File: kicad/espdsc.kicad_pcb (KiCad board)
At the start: 2 copper layers, 58.4 x 35.3 mm, 15 parts, among them J1 RJ45, P1 USB_B, SW1 Reset, SW2 Prog, U1 ESP-12E, U2 MCP1825S-3302E/DB, U3 TXB0104

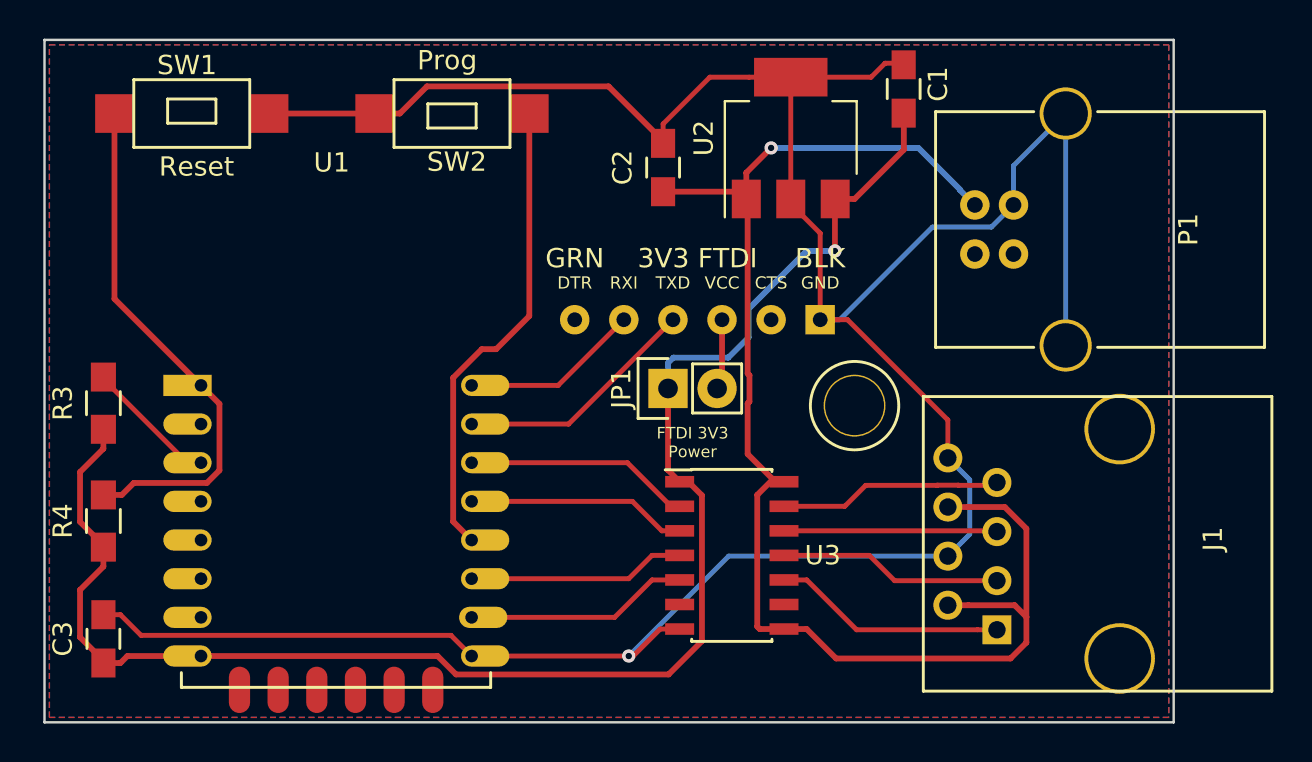
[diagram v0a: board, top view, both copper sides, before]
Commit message: update design for v1.0 release
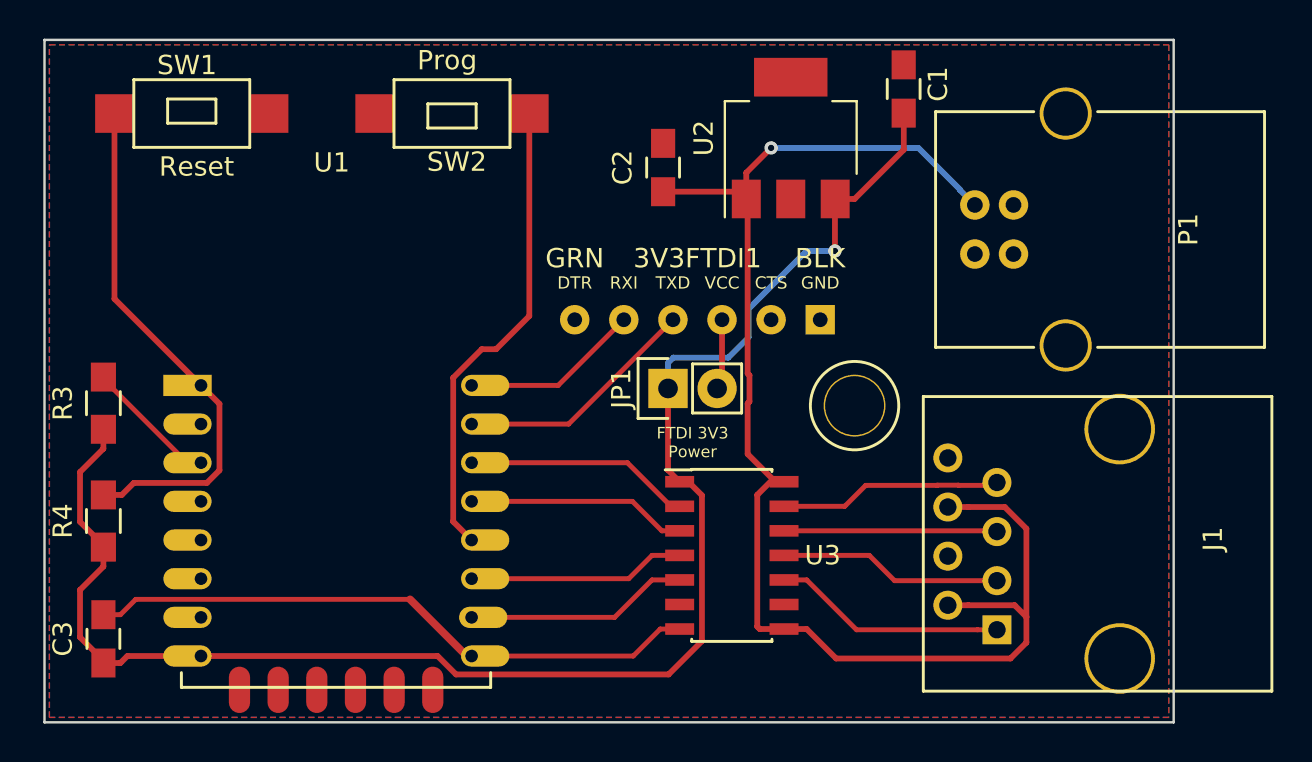
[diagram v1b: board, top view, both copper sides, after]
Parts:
- 3V3FTDI1: renamed from 3V3 FTDI
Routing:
- net GND: track 147.3 -> 31.9 mm, vias 1 -> 0
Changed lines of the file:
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@@
     (thickness 1.6)
     (drawings 6)
-    (tracks 166)
+    (tracks 131)
     (zones 0)
     (modules 15)
@@
   )
   (setup
-    (last_trace_width 0.3)
+    (last_trace_width 0.254)
     (user_trace_width 0.1524)
     (user_trace_width 0.2)
@@
   (net 15 "Net-(R3-Pad2)")
   (net 16 "Net-(R4-Pad2)")
-  (net 17 "Net-(CONN1-Pad4)")
+  (net 17 "Net-(3V3FTDI1-Pad4)")
   (net_class Default "Dit is de standaard class."
     (clearance 0.254)
@@
     (add_net +5V)
     (add_net GND)
-    (add_net "Net-(CONN1-Pad4)")
+    (add_net "Net-(3V3FTDI1-Pad4)")
     (add_net "Net-(J1-Pad1)")
     (add_net "Net-(J1-Pad3)")
@@
   (module synfinatic:FTDIHeader (layer F.Cu)
     (at 196.342 101.854)
-    (fp_text reference "3V3 FTDI" (at 0 -3.175) (layer F.SilkS)
+    (fp_text reference 3V3FTDI1 (at 0 -3.175) (layer F.SilkS)
       (effects (font (size 1 1) (thickness 0.15)))
     )
@@
       (net 5 RXD))
     (pad 4 thru_hole circle (at 1.27 0) (size 1.524 1.524) (drill 0.762) (layers *.Cu *.Mask)
-      (net 17 "Net-(CONN1-Pad4)"))
+      (net 17 "Net-(3V3FTDI1-Pad4)"))
     (pad 5 thru_hole circle (at 3.81 0) (size 1.524 1.524) (drill 0.762) (layers *.Cu *.Mask))
     (pad 6 thru_hole rect (at 6.35 0) (size 1.524 1.524) (drill 0.762) (layers *.Cu *.Mask)
@@
       (net 1 +3V3))
     (pad 2 thru_hole oval (at 0 2.54 90) (size 2.032 2.032) (drill 1.016) (layers *.Cu *.Mask)
-      (net 17 "Net-(CONN1-Pad4)"))
+      (net 17 "Net-(3V3FTDI1-Pad4)"))
     (model Pin_Headers.3dshapes/Pin_Header_Straight_1x02.wrl
       (at (xyz 0 -0.05 0))
@@
   (segment (start 166.849 119.252) (end 170.658 119.252) (width 0.3) (layer F.Cu) (net 1))
   (segment (start 166.487 119.614) (end 166.849 119.252) (width 0.3) (layer F.Cu) (net 1))
-  (segment (start 202.692 101.854) (end 204.107309 101.854) (width 0.254) (layer F.Cu) (net 2))
-  (segment (start 204.107309 101.854) (end 209.296 107.042691) (width 0.254) (layer F.Cu) (net 2))
-  (segment (start 209.296 107.042691) (end 209.296 109.0041) (width 0.254) (layer F.Cu) (net 2))
-  (segment (start 194.564 92.73) (end 194.564 92.605) (width 0.3) (layer F.Cu) (net 2))
-  (segment (start 194.564 92.605) (end 191.740999 89.781999) (width 0.3) (layer F.Cu) (net 2))
-  (segment (start 191.740999 89.781999) (end 182.346001 89.781999) (width 0.3) (layer F.Cu) (net 2))
-  (segment (start 182.346001 89.781999) (end 180.942 91.186) (width 0.3) (layer F.Cu) (net 2))
-  (segment (start 180.942 91.186) (end 179.642 91.186) (width 0.3) (layer F.Cu) (net 2))
-  (segment (start 174.18 91.186) (end 179.642 91.186) (width 0.3) (layer F.Cu) (net 2))
-  (segment (start 201.168 89.306) (end 205.325801 89.306) (width 0.254) (layer F.Cu) (net 2))
-  (segment (start 205.325801 89.306) (end 206.048188 88.583613) (width 0.254) (layer F.Cu) (net 2))
-  (segment (start 206.048188 88.583613) (end 206.584387 88.583613) (width 0.254) (layer F.Cu) (net 2))
-  (segment (start 206.584387 88.583613) (end 207.01 88.158) (width 0.254) (layer F.Cu) (net 2))
-  (segment (start 165.608 117.114) (end 166.487 117.114) (width 0.254) (layer F.Cu) (net 2))
-  (segment (start 166.487 117.114) (end 167.55601 118.18301) (width 0.254) (layer F.Cu) (net 2))
-  (segment (start 167.55601 118.18301) (end 183.58901 118.18301) (width 0.254) (layer F.Cu) (net 2))
-  (segment (start 183.58901 118.18301) (end 184.658 119.252) (width 0.254) (layer F.Cu) (net 2))
-  (segment (start 215.392 91.186) (end 212.69198 93.88602) (width 0.254) (layer B.Cu) (net 2))
-  (segment (start 212.69198 93.88602) (end 212.69198 95.91548) (width 0.254) (layer B.Cu) (net 2))
-  (segment (start 184.658 119.252) (end 192.786 119.252) (width 0.254) (layer F.Cu) (net 2))
-  (segment (start 192.786 119.252) (end 193.02 119.252) (width 0.254) (layer F.Cu) (net 2))
-  (segment (start 209.296 114.0841) (end 197.9539 114.0841) (width 0.254) (layer B.Cu) (net 2))
-  (segment (start 197.9539 114.0841) (end 192.786 119.252) (width 0.254) (layer B.Cu) (net 2))
-  (via (at 192.786 119.252) (size 0.6858) (drill 0.3302) (layers F.Cu B.Cu) (net 2))
-  (segment (start 193.02 119.252) (end 194.416 117.856) (width 0.254) (layer F.Cu) (net 2))
-  (segment (start 194.416 117.856) (end 195.42 117.856) (width 0.254) (layer F.Cu) (net 2))
-  (segment (start 194.564 92.73) (end 194.564 91.726) (width 0.254) (layer F.Cu) (net 2))
-  (segment (start 194.564 91.726) (end 196.984 89.306) (width 0.254) (layer F.Cu) (net 2))
-  (segment (start 196.984 89.306) (end 199.014 89.306) (width 0.254) (layer F.Cu) (net 2))
-  (segment (start 199.014 89.306) (end 201.168 89.306) (width 0.254) (layer F.Cu) (net 2))
-  (segment (start 201.168 89.306) (end 201.168 95.606) (width 0.254) (layer F.Cu) (net 2))
-  (segment (start 202.692 101.854) (end 202.692 97.38) (width 0.254) (layer F.Cu) (net 2))
-  (segment (start 202.692 97.38) (end 201.168 95.856) (width 0.254) (layer F.Cu) (net 2))
-  (segment (start 201.168 95.856) (end 201.168 95.606) (width 0.254) (layer F.Cu) (net 2))
-  (segment (start 212.69198 95.91548) (end 211.548979 97.058481) (width 0.254) (layer B.Cu) (net 2))
-  (segment (start 203.708 101.854) (end 202.692 101.854) (width 0.254) (layer B.Cu) (net 2))
-  (segment (start 208.503519 97.058481) (end 203.708 101.854) (width 0.254) (layer B.Cu) (net 2))
-  (segment (start 211.548979 97.058481) (end 208.503519 97.058481) (width 0.254) (layer B.Cu) (net 2))
-  (segment (start 209.296 109.0041) (end 210.427571 110.135671) (width 0.254) (layer B.Cu) (net 2))
-  (segment (start 210.427571 110.135671) (end 210.427571 112.952529) (width 0.254) (layer B.Cu) (net 2))
-  (segment (start 210.427571 112.952529) (end 210.046569 113.333531) (width 0.254) (layer B.Cu) (net 2))
-  (segment (start 210.046569 113.333531) (end 209.296 114.0841) (width 0.254) (layer B.Cu) (net 2))
-  (segment (start 215.392 91.186) (end 215.392 103.18496) (width 0.254) (layer B.Cu) (net 2))
+  (segment (start 195.42 117.856) (end 194.416 117.856) (width 0.254) (layer F.Cu) (net 2))
+  (segment (start 194.416 117.856) (end 193.02 119.252) (width 0.254) (layer F.Cu) (net 2))
+  (segment (start 193.02 119.252) (end 184.658 119.252) (width 0.254) (layer F.Cu) (net 2))
+  (segment (start 184.403 119.252) (end 181.47199 116.32099) (width 0.4) (layer F.Cu) (net 2))
+  (segment (start 181.47199 116.32099) (end 167.28001 116.32099) (width 0.254) (layer F.Cu) (net 2))
+  (segment (start 167.28001 116.32099) (end 166.487 117.114) (width 0.254) (layer F.Cu) (net 2))
+  (segment (start 166.487 117.114) (end 165.608 117.114) (width 0.254) (layer F.Cu) (net 2))
+  (segment (start 184.658 119.252) (end 184.403 119.252) (width 0.254) (layer F.Cu) (net 2))
   (segment (start 198.868 95.606) (end 198.937648 95.675648) (width 0.3) (layer F.Cu) (net 3))
   (segment (start 198.937648 95.675648) (end 198.937648 104.634046) (width 0.3) (layer F.Cu) (net 3))

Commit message: v1.1 board & code
- Move GPIO2/15 to GPIO14/12 to avoid boot conflict
- Remove level shifter and replace with 4x 150Ohm resistors
- Tweak RJ45 footprint for better fit
- Add pullup for D+ on USB
- Remove 3.3V FTDI jumper
- Move Reset button label
- FTDI no longer can provide power
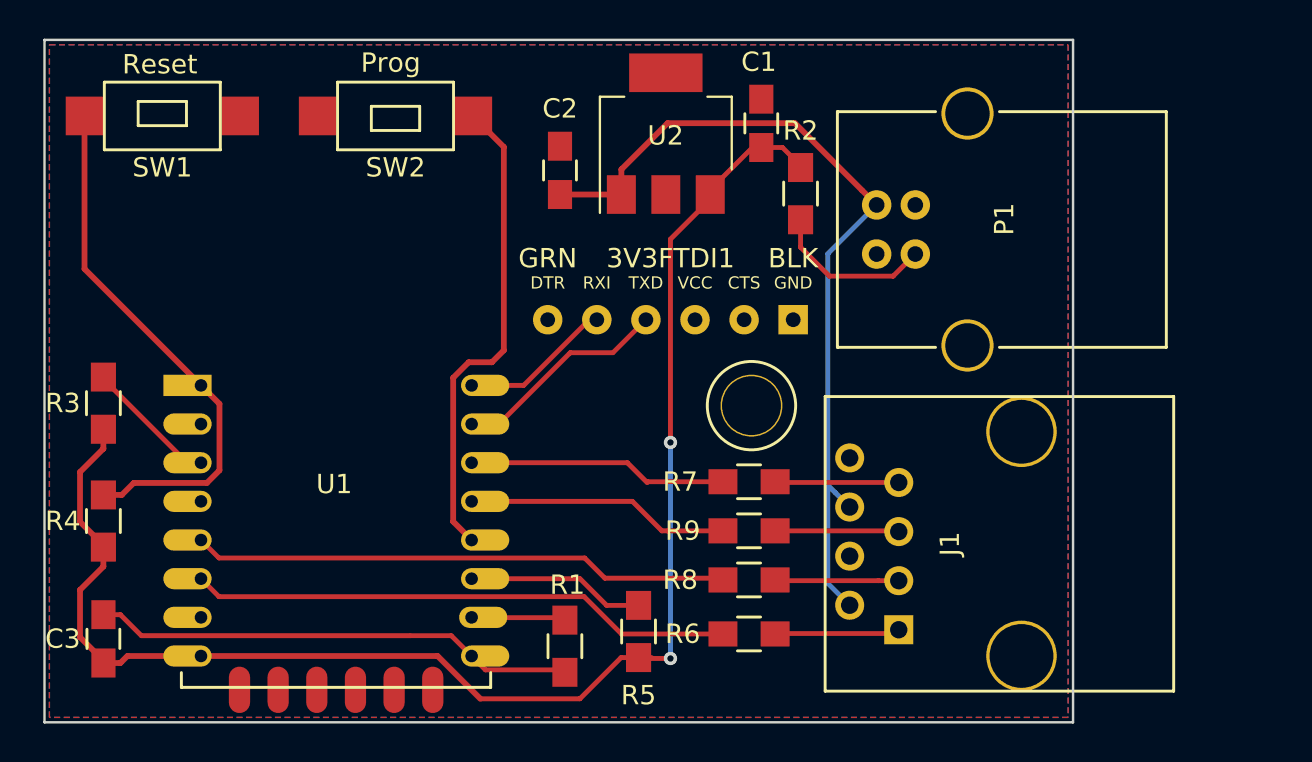
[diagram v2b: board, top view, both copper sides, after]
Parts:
- removed JP1: Jumper_NO_Small, Pin_Headers:Pin_Header_Straight_1x02
- removed U3: TXB0104, Housings_SOIC:SOIC-14_3.9x8.7mm_Pitch1.27mm
- added R1: 4.7k, Resistors_SMD:R_0805_HandSoldering, F.Cu at (189.5, 118.7)
- added R2: 1.5k, Resistors_SMD:R_0805_HandSoldering, F.Cu at (201.7, 95.3)
- added R5: 1k, Resistors_SMD:R_0805_HandSoldering, F.Cu at (193.3, 118.0)
- added R6: 510, Resistors_SMD:R_0805_HandSoldering, F.Cu at (199.0, 118.1)
- added R7: 510, Resistors_SMD:R_0805_HandSoldering, F.Cu at (199.0, 110.2)
- added R8: 510, Resistors_SMD:R_0805_HandSoldering, F.Cu at (199.0, 115.3)
- added R9: 510, Resistors_SMD:R_0805_HandSoldering, F.Cu at (199.0, 112.8)
- J1: footprint Connectors:RJ45_8 -> synfinatic:RJ45_8
- moved C1 7.58 mm to (199.6, 91.7)
- moved U2 6.47 mm to (194.7, 92.2)
- moved C2 5.34 mm to (189.2, 94.1)
- moved ? 5.33 mm to (199.1, 106.3)
- moved J1 5.08 mm to (213.1, 113.4)
- moved P1 5.08 mm to (205.6, 95.9)
- moved SW2 2.92 mm to (180.7, 91.3)
- moved SW1 1.53 mm to (168.7, 91.3)
- moved 3V3FTDI1 1.40 mm to (194.9, 101.9)
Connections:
- 3V3FTDI1 pad 1: (no net) -> Net-(3V3FTDI1-Pad1)
- 3V3FTDI1 pad 5: (no net) -> Net-(3V3FTDI1-Pad5)
- P1 pad 2: (no net) -> Net-(P1-Pad2)
- P1 pad 3: (no net) -> Net-(P1-Pad3)
- U1 pad 17: (no net) -> Net-(U1-Pad17)
- U1 pad 18: (no net) -> Net-(U1-Pad18)
- U1 pad 19: (no net) -> Net-(U1-Pad19)
- U1 pad 2: (no net) -> Net-(U1-Pad2)
- U1 pad 20: (no net) -> Net-(U1-Pad20)
- U1 pad 21: (no net) -> Net-(U1-Pad21)
- U1 pad 22: (no net) -> Net-(U1-Pad22)
- U1 pad 4: (no net) -> Net-(U1-Pad4)
- U1 pad 5: (no net) -> Net-(R8-Pad2)
- U1 pad 6: (no net) -> Net-(R6-Pad2)
- U1 pad 7: (no net) -> Net-(U1-Pad7)
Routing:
- net Net-(R6-Pad2): track 0.00 -> 28.3 mm
- net Net-(R8-Pad2): track 0.00 -> 28.0 mm
- net +5V: track 72.1 -> 44.3 mm, vias 1 -> 0
- net Net-(P1-Pad3): track 0.00 -> 8.45 mm
- net GND: track 31.9 -> 25.3 mm
- net +3V3: track 83.4 -> 77.3 mm, vias 1 -> 2
- net Net-(R1-Pad1): track 11.0 -> 4.83 mm
- net Net-(J1-Pad1): track 11.7 -> 6.63 mm
- net Net-(J1-Pad3): track 11.2 -> 6.34 mm
- net Net-(J1-Pad7): track 11.2 -> 6.41 mm
- net Net-(J1-Pad5): track 10.7 -> 6.41 mm
- net Net-(3V3FTDI1-Pad4): track 3.66 -> 0.00 mm
- net Net-(R9-Pad2): track 10.8 -> 13.7 mm
- net Net-(R7-Pad2): track 11.7 -> 13.4 mm
- net TXD: track 9.28 -> 7.74 mm
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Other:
- board size 58.4 x 35.3 mm -> 53.2 x 35.3 mm
- board text added: "ESP-DSC v1.1 https://synfin.net/espdsc 20171202"
- board text removed: "ESP-DSC v1.0 https://synfin.net/espdsc 20170226"
- board text removed: "FTDI 3V3 Power"

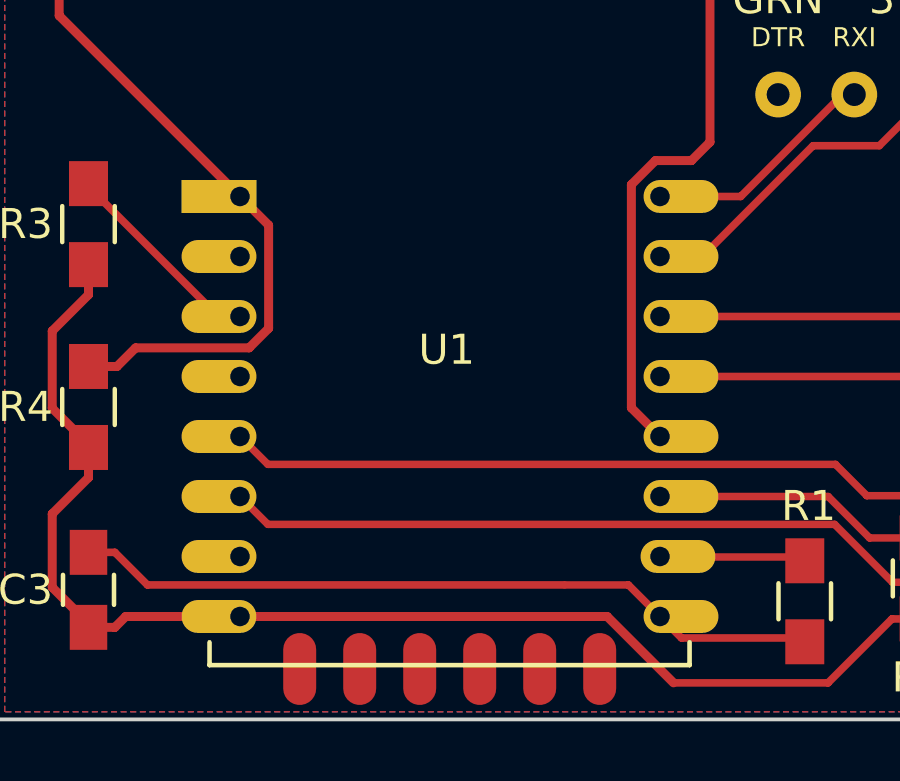
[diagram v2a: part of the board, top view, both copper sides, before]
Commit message: v1.2
- Switch ESP12E to pure SMD footprint
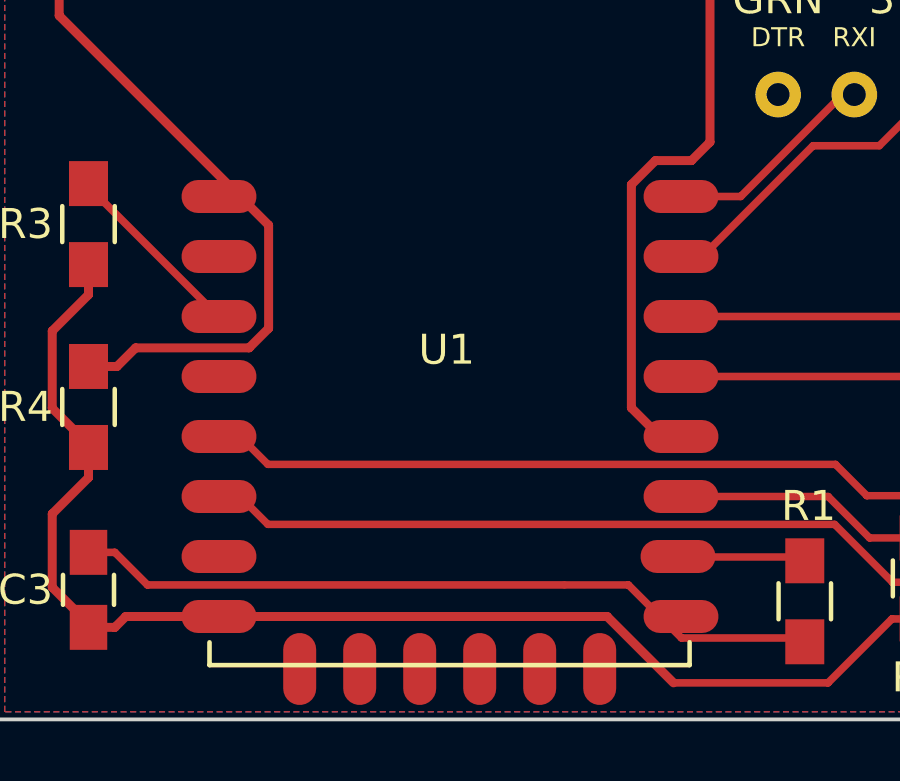
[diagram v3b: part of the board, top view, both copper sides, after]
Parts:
- U1: footprint ESP8266:ESP-12E -> synfinatic:ESP-12E-SMD
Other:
- board text added: "ESP-DSC v1.2 https://synfin.net/espdsc 20171203"
- board text removed: "ESP-DSC v1.1 https://synfin.net/espdsc 20171202"
